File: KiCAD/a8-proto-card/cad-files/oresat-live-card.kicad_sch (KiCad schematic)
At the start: 0 parts

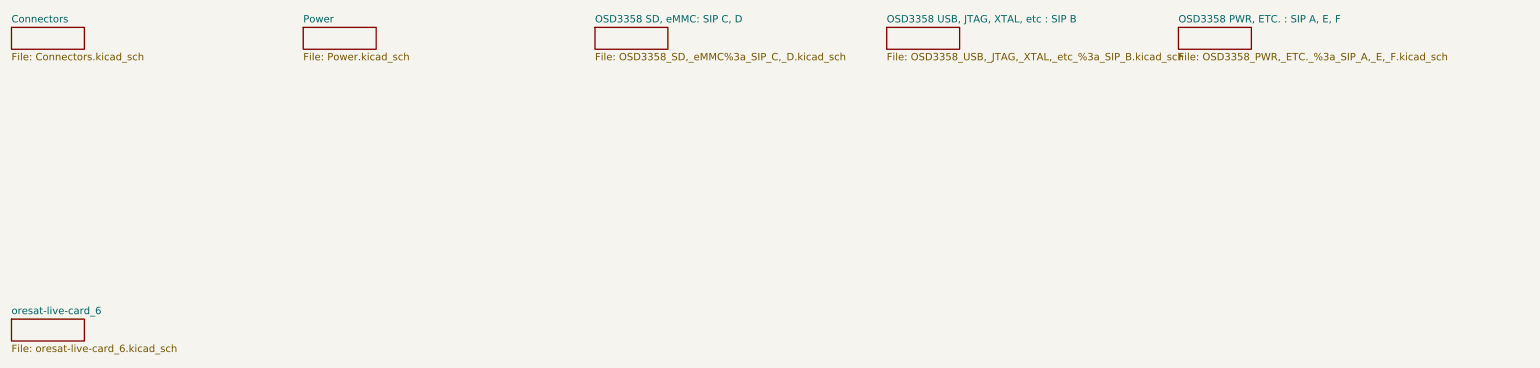
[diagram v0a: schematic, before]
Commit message: removed page 6; edited connectors, PWR and SD reader schematic
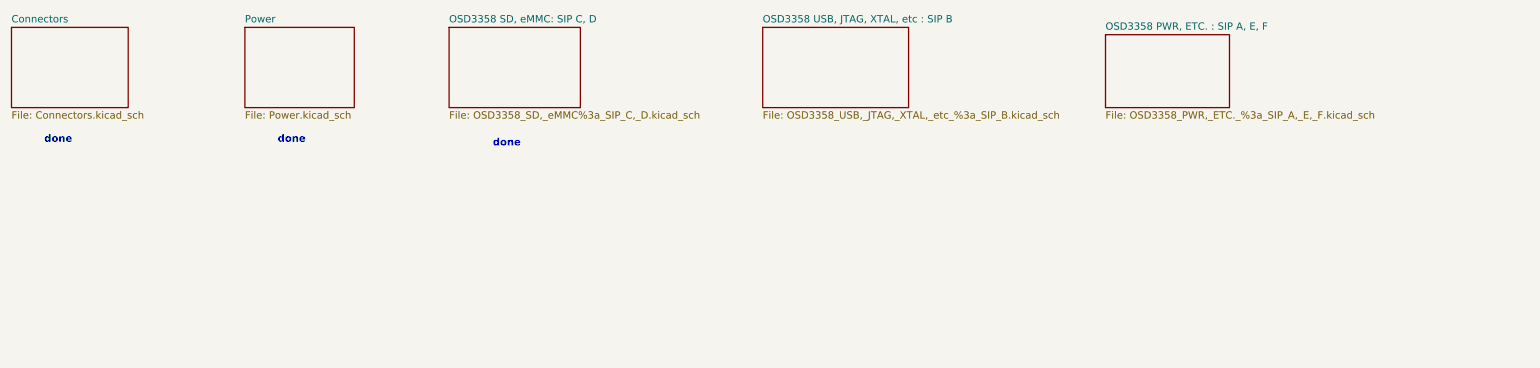
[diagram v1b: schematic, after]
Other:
- removed sheet oresat-live-card_6
- note added: "done"
